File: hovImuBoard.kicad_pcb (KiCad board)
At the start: 2 copper layers, 71.6 x 71.6 mm, 67 parts, among them J1 AVR-ISP-6, J2 Ext. Power, J3 54602-908LF, J4 AVR-JTAG-10, J5 ExtensionPort, J6 Debug, U1 LD2981, U2 BMX160, U3 SN65HVD32DR, U4 ATmega1284P-AU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

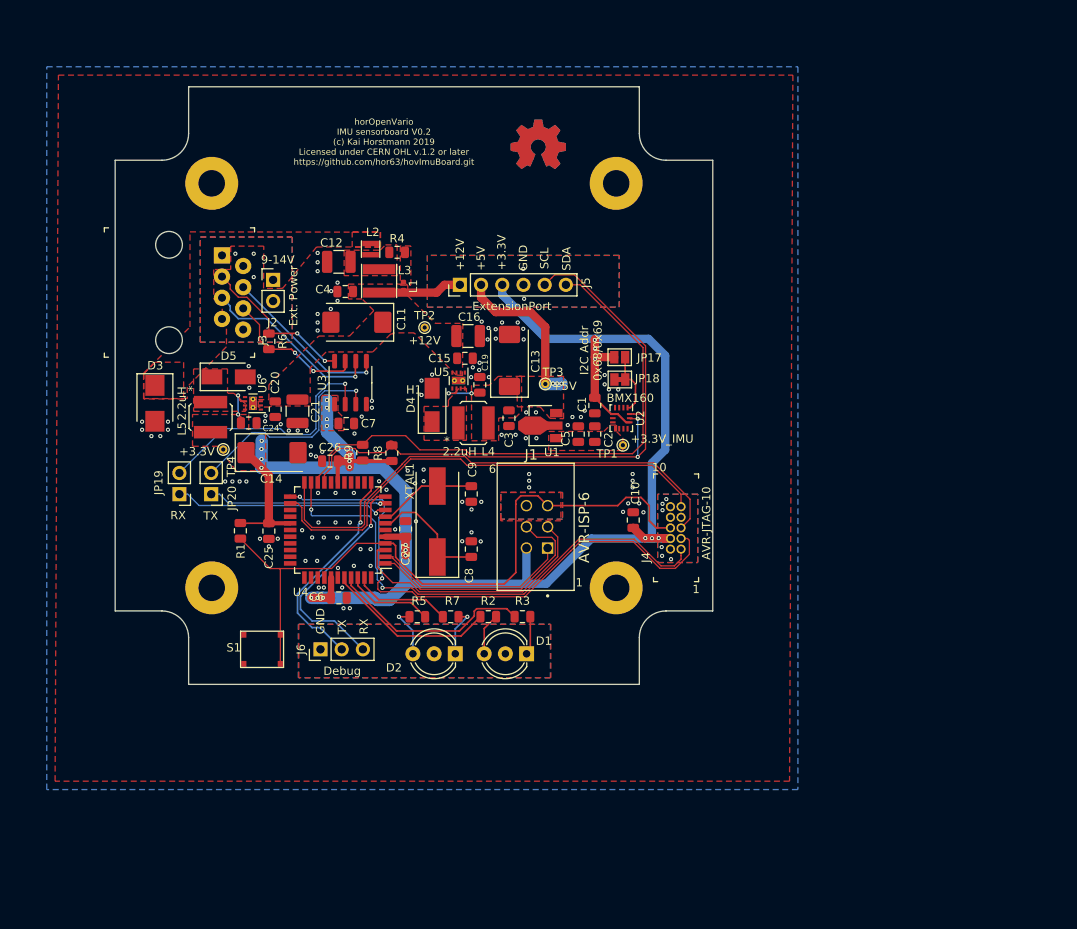
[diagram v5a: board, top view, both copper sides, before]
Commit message: WIP: Redesign of the sensor board.
Major re-design:
- LVDS instead of RS422 driver
- Simplify buck converter design.
- Make the back-plane mostly un-interrupted.
- Smaller cpacitors, eliminate tantal capacitors.
- Make ESD diode smaller.
- Pick different parts.
- Smaller LEDs.
- Eliminate the diodes at the buck converters.
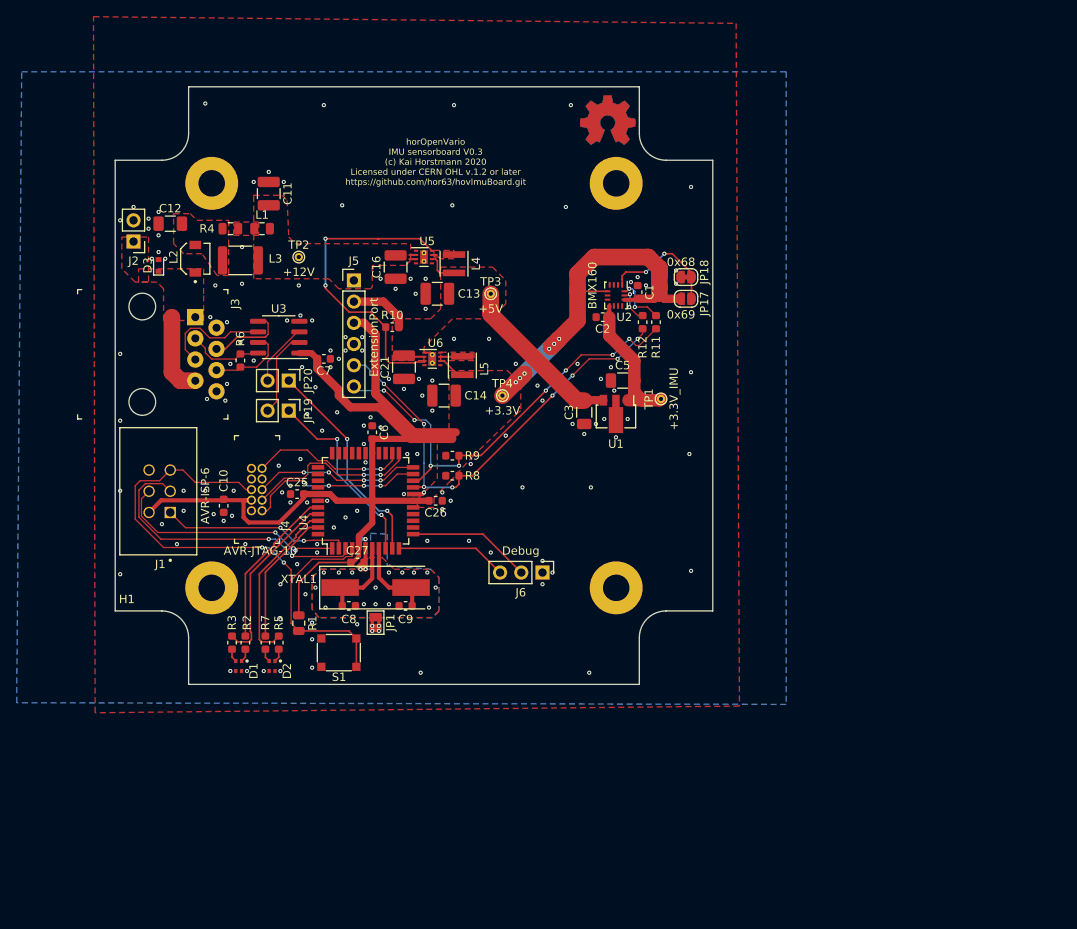
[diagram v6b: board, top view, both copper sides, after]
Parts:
- removed C15, C19, C20, C24, C4: 220nF, Capacitor_SMD:C_0805_2012Metric
- removed D4, D5: B120-E3, Diode_SMD:D_SMA
- added JP1: SolderJumper_2_Bridged, Jumper:SolderJumper-2_P1.3mm_Bridged2Bar_Pad1.0x1.5mm, F.Cu at (96.4, 120.0)
- added R10: 100k, Resistor_SMD:R_0603_1608Metric, F.Cu at (98.4, 84.6)
- added R11: 47, Resistor_SMD:R_0603_1608Metric, F.Cu at (130.0, 84.0)
- added R12: 47, Resistor_SMD:R_0603_1608Metric, F.Cu at (128.4, 84.0)
- C1, C10, C2, C25, C26, C27, C6, C7: value 220nF -> 100nF; footprint Capacitor_SMD:C_0805_2012Metric -> Capacitor_SMD:C_0603_1608Metric
- C11, C13, C14: value 47uF -> 22uF; footprint Capacitor_Tantalum_SMD:CP_EIA-7343-31_Kemet-D -> Capacitor_SMD:C_1210_3225Metric
- C12: value 10uF -> 4.7uF; footprint Capacitor_SMD:C_1210_3225Metric -> Capacitor_SMD:C_1206_3216Metric
- C3: value 220nF -> 4.7uF; footprint Capacitor_SMD:C_0805_2012Metric -> Capacitor_SMD:C_1206_3216Metric
- C5: value 2.2uF -> 4.7uF; footprint Capacitor_SMD:C_0805_2012Metric -> Capacitor_SMD:C_1206_3216Metric
- C8, C9: footprint Capacitor_SMD:C_0805_2012Metric -> Capacitor_SMD:C_0603_1608Metric
- D1, D2: value LED_Dual_ACA -> LED Green/Red; footprint LED_THT:LED_D5.0mm-3 -> hovImuBoard:LED_APHB1608LZGKSURKC
- D3: value P6SMB18A -> VESD16C1-02V-G3-08; footprint Diode_SMD:D_SMB -> Diode_SMD:D_SOD-523
- JP17: footprint Jumper:SolderJumper-2_P1.3mm_Open_Pad1.0x1.5mm -> Jumper:SolderJumper-2_P1.3mm_Open_RoundedPad1.0x1.5mm
- JP18: footprint Jumper:SolderJumper-2_P1.3mm_Bridged_Pad1.0x1.5mm -> Jumper:SolderJumper-2_P1.3mm_Bridged_RoundedPad1.0x1.5mm
- L1: value 100nH -> 240nH; footprint Inductor_SMD:L_0402_1005Metric -> Inductor_SMD:L_0805_2012Metric
- L2: value 470nH -> 1.2uH; footprint Inductor_SMD:L_Taiyo-Yuden_NR-20xx -> hovImuBoard:IND_1231AS-H-1R2N=P3
- L3: value 3.3uH -> 8.2uH; footprint Inductor_SMD:L_Taiyo-Yuden_NR-40xx -> Inductor_SMD:L_1812_4532Metric
- L4, L5: footprint hovImuBoard:NRS5040T220MMGKV -> hovImuBoard:IND_LQH3NPN2R2MMEL
- R2, R5: value 200 -> 330; footprint Resistor_SMD:R_0805_2012Metric -> Resistor_SMD:R_0603_1608Metric
- R3, R7: value 200 -> 787; footprint Resistor_SMD:R_0805_2012Metric -> Resistor_SMD:R_0603_1608Metric
- R4: value 110m -> 180m
- R6: value 150 -> 100; footprint Resistor_SMD:R_0805_2012Metric -> Resistor_SMD:R_0603_1608Metric
- R8, R9: footprint Resistor_SMD:R_0805_2012Metric -> Resistor_SMD:R_0603_1608Metric
- U3: value SN65HVD32DR -> SN65LVDS179DR; footprint Package_SO:SO-8_3.9x4.9mm_P1.27mm -> Package_SO:SOIC-8_3.9x4.9mm_P1.27mm
- moved J4 50.4 mm to (82.8, 106.6)
- moved C10 49.1 mm to (78.2, 106.0), turned to 90 degrees
- moved J1 45.4 mm to (71.8, 106.8)
- moved R3 34.9 mm to (79.2, 122.4), turned to 90 degrees
- moved D1 34.5 mm to (80.0, 125.2), turned to 270 degrees
- moved TP4 34.1 mm to (111.6, 92.8)
- moved L5 30.8 mm to (106.8, 89.2)
- moved R2 29.3 mm to (80.8, 122.4), turned to 90 degrees
- moved J6 28.1 mm to (116.4, 114.0), turned to 270 degrees
- moved R7 22.4 mm to (83.2, 122.4), turned to 90 degrees
- moved U6 22.1 mm to (103.2, 88.4), turned to 0 degrees
- moved D2 22.0 mm to (84.0, 125.2), turned to 270 degrees
- moved C14 21.7 mm to (104.6, 92.8)
- moved L2 21.0 mm to (74.8, 76.4), turned to 90 degrees
- moved C12 20.7 mm to (71.8, 72.2)
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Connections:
- C11 pad 1: +12V -> GND
- C11 pad 2: GND -> +12V
- C13 pad 1: +5V -> GND
- C13 pad 2: GND -> +5V
- C14 pad 1: +3V3 -> GND
- C14 pad 2: GND -> +3V3
- C21 pad 2: +12V -> +5V
- C8 pad 1: GND -> Net-(C8-Pad1)
- C9 pad 1: GND -> Net-(C8-Pad1)
- R2 pad 1: Net-(D1-Pad3) -> Net-(D1-Pad1)
- R3 pad 1: Net-(D1-Pad1) -> Net-(D1-Pad3)
- R5 pad 1: Net-(D2-Pad3) -> Net-(D2-Pad1)
- R7 pad 1: Net-(D2-Pad1) -> Net-(D2-Pad3)
- U2 pad 13: /SCL -> Net-(R12-Pad2)
- U2 pad 14: /SDA -> Net-(R11-Pad2)
- U5 pad 8: (no net) -> Net-(R10-Pad1)
- U6 pad 2: +12V -> +5V
- U6 pad 3: +12V -> Net-(R10-Pad1)
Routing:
- net /JTAG_TDO: track 68.1 -> 21.0 mm
- net /JTAG_TMS: track 62.2 -> 20.0 mm, vias 0 -> 4
- net /JTAG_TCK: track 61.8 -> 21.2 mm, vias 2 -> 4
- net /JTAG_TDI: track 58.1 -> 18.8 mm, vias 0 -> 2
- net Net-(R10-Pad1): track 0.00 -> 37.4 mm, vias 0 -> 2
- net +3V3: track 201.8 -> 173.3 mm, vias 25 -> 6
- net /SCL: track 77.2 -> 55.2 mm, vias 2 -> 8
- net /RX: track 29.6 -> 10.3 mm, vias 1 -> 0
- net /TX: track 25.9 -> 7.55 mm, vias 1 -> 0
- net /3.3V_IMU: track 0.00 -> 16.9 mm
- net /SDA: track 69.9 -> 54.6 mm, vias 0 -> 8
- net /RX_DBG: track 27.7 -> 13.3 mm, vias 1 -> 0
- net /MCU_RESET: track 81.5 -> 69.0 mm, vias 0 -> 2
- net /TX_DBG: track 26.4 -> 14.9 mm, vias 1 -> 0
- net /TX+: track 20.3 -> 9.55 mm, vias 1 -> 0
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- added copper zone on B.Cu, net Net-(C8-Pad1)
- added copper zone on F.Cu, net Net-(C8-Pad1)
- removed copper zone on F.Cu, net /3.3V_IMU
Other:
- board text added: "horOpenVario IMU sensorboard V0.3 (c) Kai Horstmann 2020 Licensed under CERN OHL v.1.2 or later https://github.com/hor63/hovImuBoard.git"
- board text removed: "+12V"
- board text removed: "+3.3V"
- board text removed: "+5V"
- board text removed: "1"
- board text removed: "10"
- board text removed: "6"
- board text removed: "9-14V"
- board text removed: "GND"
- board text removed: "I2C Addr 0x68/0x69"
- board text removed: "RX"
- board text removed: "SCL"
- board text removed: "SDA"
- board text removed: "TX"
- board text removed: "horOpenVario IMU sensorboard V0.2 (c) Kai Horstmann 2019 Licensed under CERN OHL v.1.2 or later https://github.com/hor63/hovImuBoard.git"

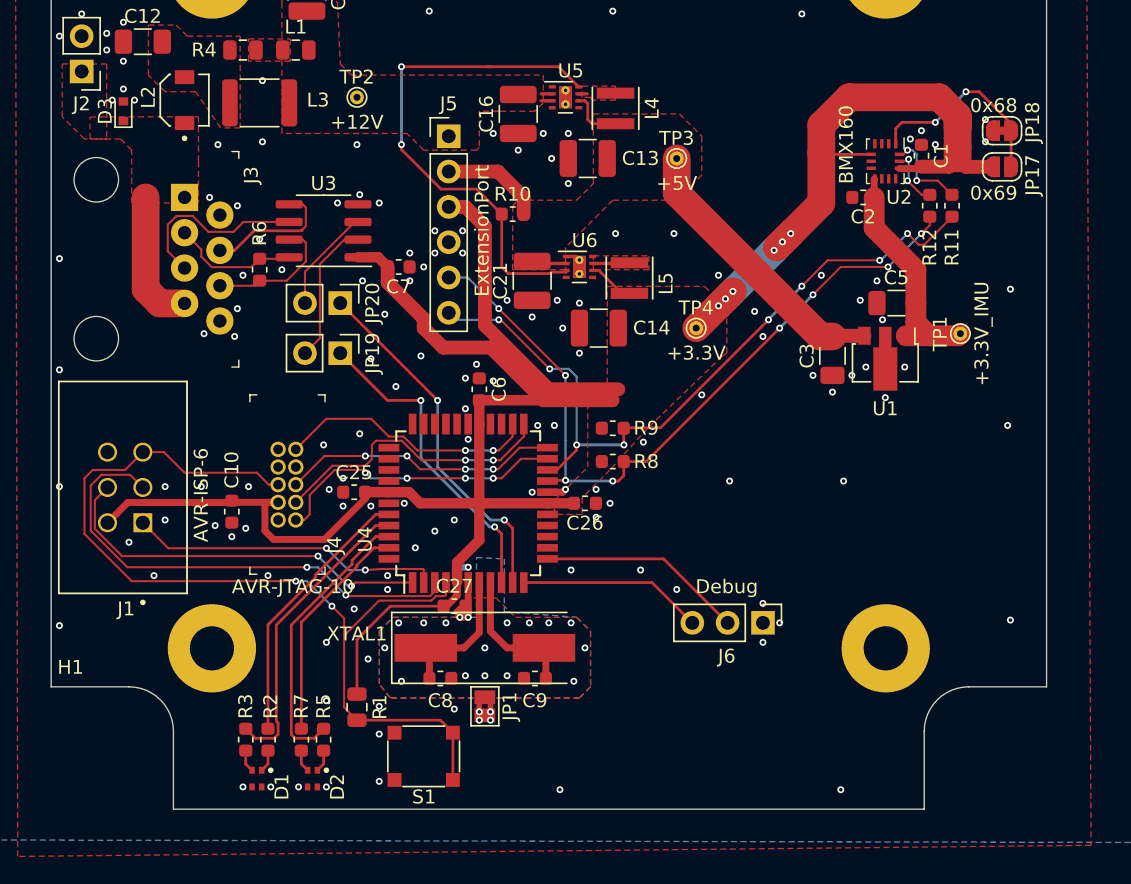
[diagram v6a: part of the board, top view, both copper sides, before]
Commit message: Complete re-design of hovImuBoard
- Create a proper local ground plane for the oscillator
- Create a local ground plane for the analog and digital ground.
- Clean separation of VDD and VDDIO, and ground lines for I/O.
- Hook up INT1 of the IMU with pin 15 of the MCU
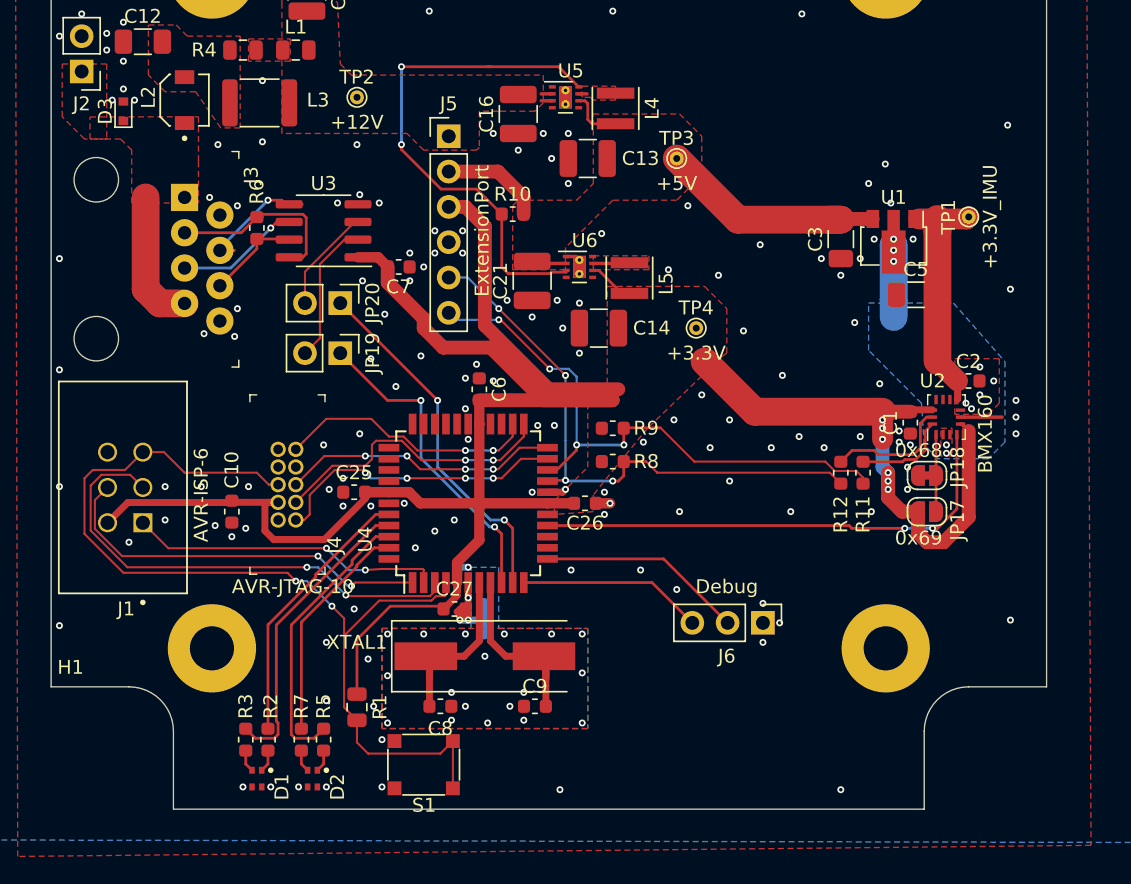
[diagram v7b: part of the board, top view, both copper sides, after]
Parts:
- removed JP1: SolderJumper_2_Bridged, Jumper:SolderJumper-2_P1.3mm_Bridged2Bar_Pad1.0x1.5mm
- added NT1: Net-Tie_2, NetTie:NetTie-2_SMD_Pad2.0mm, B.Cu at (125.8, 88.8)
- added NT2: Net-Tie_2, NetTie:NetTie-2_SMD_Pad0.5mm, B.Cu at (95.6, 113.8)
- moved JP18 25.4 mm to (128.2, 103.4)
- moved JP17 25.4 mm to (128.2, 106.0)
- moved R11 20.2 mm to (123.6, 103.2)
- moved R12 20.2 mm to (122.0, 103.2)
- moved C1 19.2 mm to (127.0, 99.6), turned to 90 degrees
- moved U2 18.9 mm to (129.6, 99.2), turned to 90 degrees
- moved C2 15.2 mm to (131.2, 96.6), turned to 180 degrees
- moved TP1 8.42 mm to (131.2, 84.8)
- moved U1 8.42 mm to (125.8, 86.6)
- moved C3 8.42 mm to (122.0, 86.4)
- moved R6 3.01 mm to (80.0, 85.6)
- moved C8 2.00 mm to (93.2, 120.0)
- moved C9 2.00 mm to (100.0, 120.0)
- moved C5 1.52 mm to (127.4, 90.4)
- moved S1 0.60 mm to (92.0, 124.2)
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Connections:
- net Net-(C8-Pad1) renamed GND_OSC
- C2 pad 1: GND -> GND_BMX160
- U2 pad 2: GND -> GND_BMX160
- U2 pad 3: GND -> GND_BMX160
- U2 pad 4: (no net) -> /DATA_READY
- U2 pad 7: GND -> GND_BMX160
- U4 pad 15: (no net) -> /DATA_READY
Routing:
- net /DATA_READY: track 0.00 -> 35.5 mm, vias 0 -> 2
- net /SCL: track 55.2 -> 41.8 mm, vias 8 -> 4
- net /SDA: track 54.6 -> 43.1 mm, vias 8 -> 4
- net Net-(JP17-Pad2): track 14.1 -> 5.54 mm, vias 2 -> 0
- net Net-(R12-Pad2): track 4.51 -> 9.39 mm, vias 2 -> 0
- net /RX+: track 9.15 -> 13.9 mm
- net GND: track 7.57 -> 12.2 mm, vias 151 -> 157
- net /TX-: track 13.4 -> 8.90 mm, vias 0 -> 1
- net Net-(C9-Pad2): track 10.2 -> 14.5 mm
- net Net-(C8-Pad2): track 10.3 -> 14.6 mm
- net +5V: track 34.2 -> 30.7 mm
- net /RX-: track 9.55 -> 6.81 mm
- net GND_OSC: track 0.00 -> 2.00 mm, vias 15 -> 18
- net +3V3: track 173.3 -> 175.0 mm
- net /MCU_RESET: track 69.0 -> 70.6 mm
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- added copper zone on B.Cu, net GND_BMX160
- added copper zone on F.Cu, net GND_BMX160

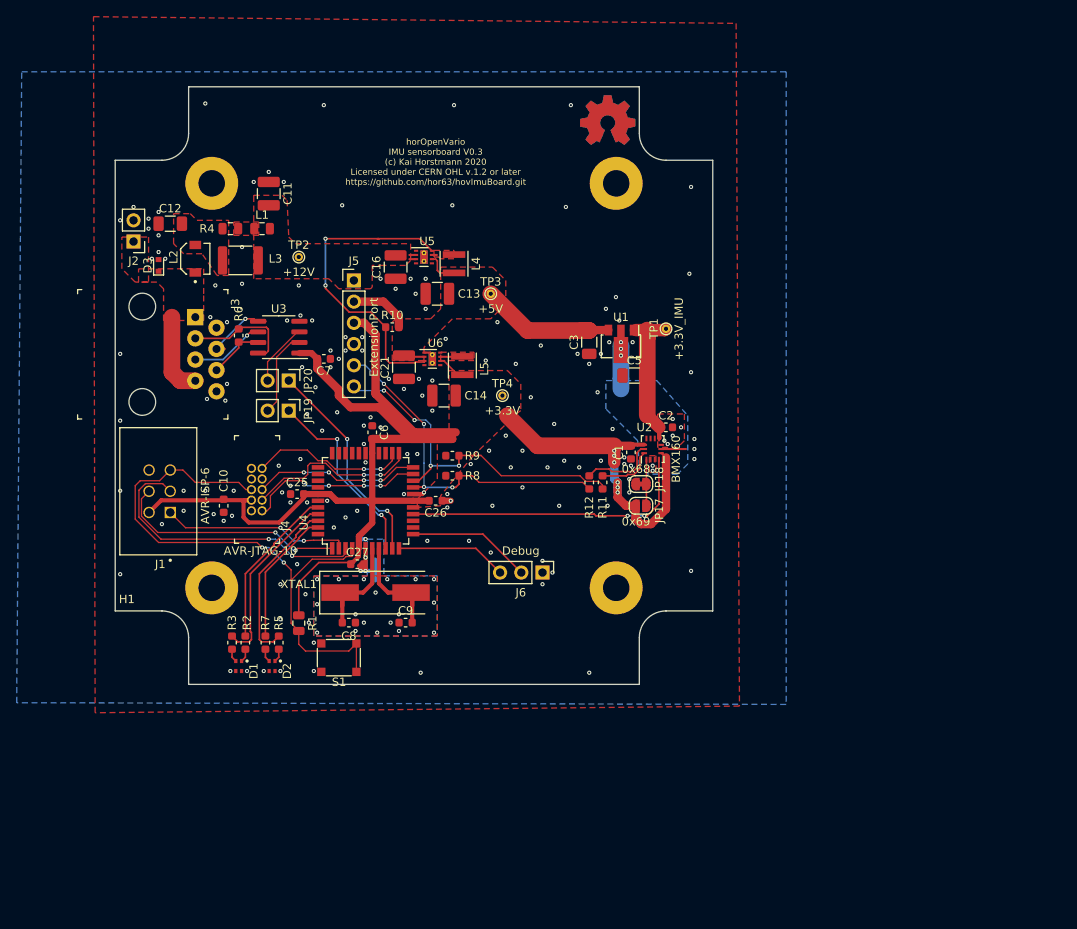
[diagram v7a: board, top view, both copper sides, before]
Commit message: Rev. is 0.3, minor trace optimiztions.
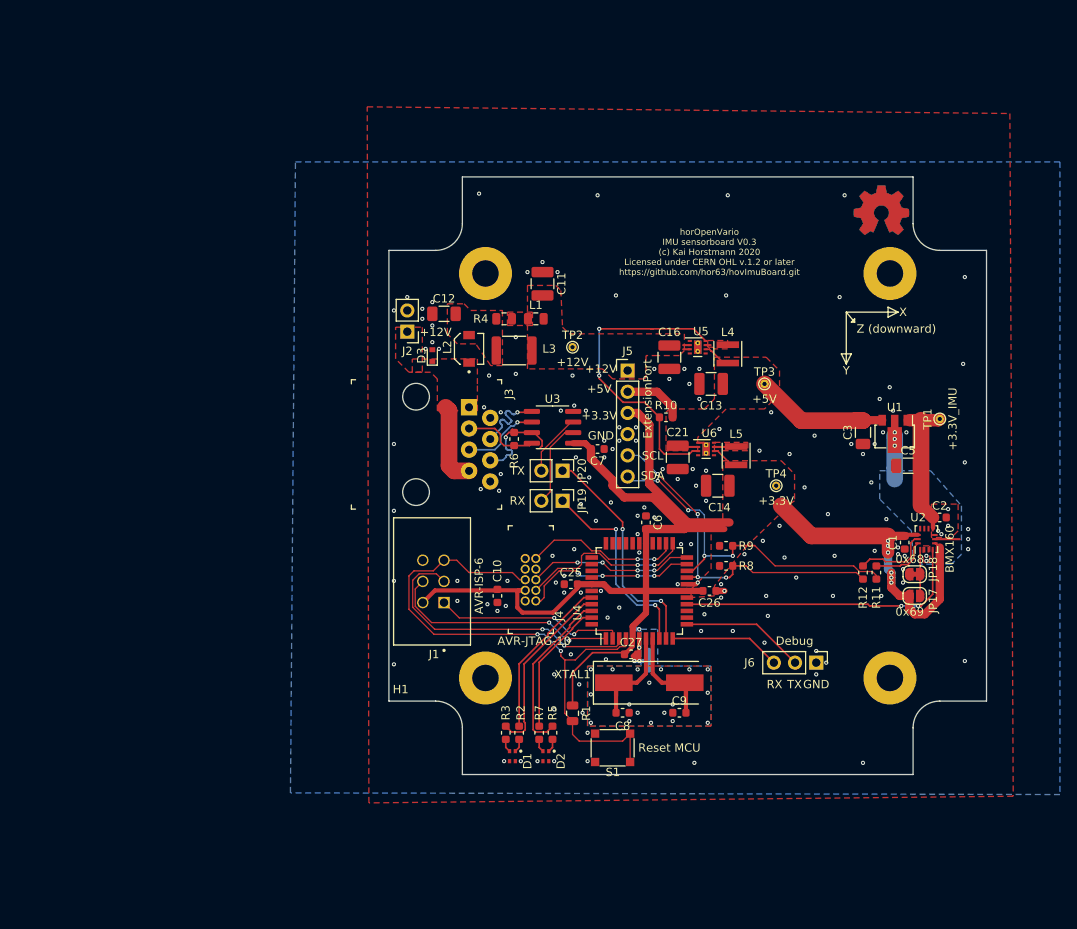
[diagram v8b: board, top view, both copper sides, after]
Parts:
- moved R6 35.3 mm to (113.0, 98.0), turned to 90 degrees
- moved C1 34.5 mm to (159.8, 110.4)
- moved C11 34.5 mm to (116.4, 79.4)
- moved C2 34.5 mm to (164.0, 107.4)
- moved C9 34.5 mm to (132.8, 130.8)
- moved H1 34.5 mm to (133.8, 102.4)
- moved C14 34.5 mm to (137.4, 103.6)
- moved C26 34.5 mm to (136.4, 116.2)
- moved C3 34.5 mm to (154.8, 97.2)
- moved C6 34.5 mm to (128.8, 108.0)
- moved JP17 34.5 mm to (161.0, 116.8)
- moved JP18 34.5 mm to (161.0, 114.2)
- moved NT2 34.5 mm to (128.4, 124.6)
- moved R11 34.5 mm to (156.4, 114.0)
- moved R12 34.5 mm to (154.8, 114.0)
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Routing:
- net +3V3: track 175.0 -> 165.0 mm
- net /RX-: track 6.81 -> 11.7 mm, vias 0 -> 1
- net /RX+: track 13.9 -> 9.20 mm
- net Net-(JP20-Pad1): track 25.8 -> 27.5 mm
- net Net-(JP19-Pad1): track 22.9 -> 24.4 mm
- net /TX+: track 8.72 -> 9.43 mm
- net +5V: track 30.7 -> 30.0 mm
- net /TX-: track 8.90 -> 9.43 mm
- net GND: track 12.2 -> 11.8 mm, vias 157 -> 154
- net GND_BMX160: vias 7 -> 6
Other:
- board text added: "+12V"
- board text added: "+3.3V"
- board text added: "+5V"
- board text added: "GND"
- board text added: "RX"
- board text added: "Reset MCU"
- board text added: "SCL"
- board text added: "SDA"
- board text added: "TX"
- board text added: "X"
- board text added: "Y"
- board text added: "Z (downward)"
